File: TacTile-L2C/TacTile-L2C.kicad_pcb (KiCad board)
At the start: 2 copper layers, 25 x 25 mm, 2 parts, among them J1 Conn_01x05, J2 Conn_01x05

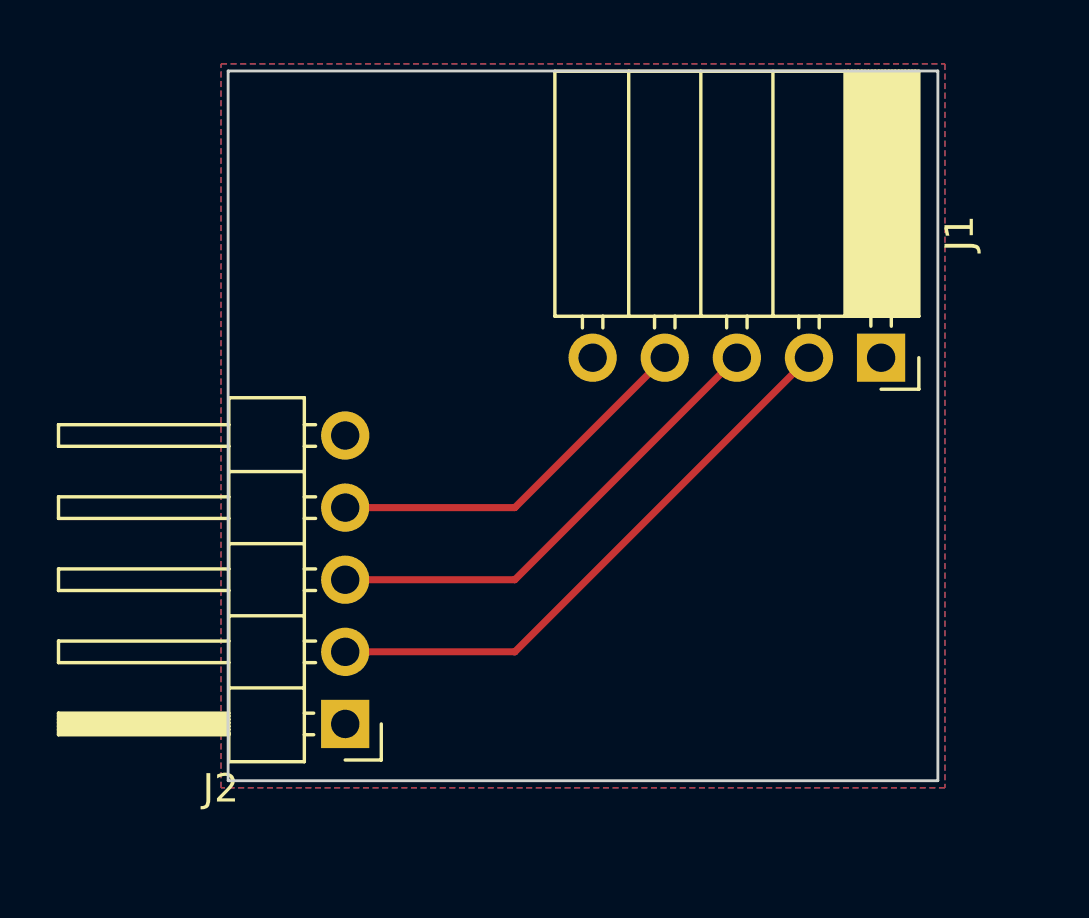
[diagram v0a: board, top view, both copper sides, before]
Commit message: Adjusted mounting for laser boards
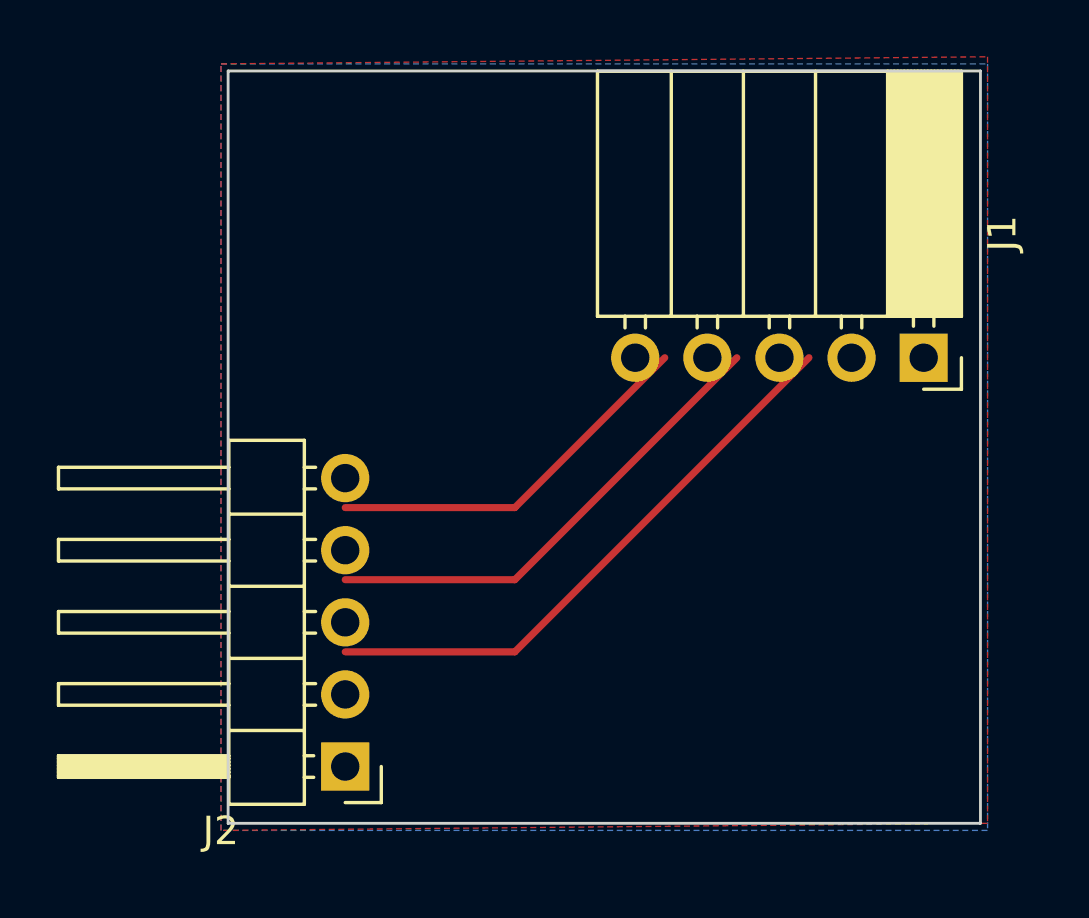
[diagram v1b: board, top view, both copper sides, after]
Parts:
- moved J1 1.50 mm to (49.5, 35.1)
- moved J2 1.50 mm to (29.1, 49.5)
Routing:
- net /SER: track 20.6 -> 0.00 mm
- net /VCC: track 0.00 -> 13.4 mm
- net /GND: track 13.4 -> 17.0 mm
- net /CLK: track 17.0 -> 20.6 mm
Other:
- board size 25 x 25 mm -> 26.5 x 26.5 mm
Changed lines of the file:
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@@
   (net 5 "/OUT")
   (footprint "Connector_PinSocket_2.54mm:PinSocket_1x05_P2.54mm_Horizontal" (layer "F.Cu")
-    (at 48 35.1 -90)
+    (at 49.5 35.1 -90)
     (descr "Through hole angled socket strip, 1x05, 2.54mm pitch, 8.51mm socket length, single row (from Kicad 4.0.7), script generated")
     (tags "Through hole angled socket strip THT 1x05 2.54mm single row")
@@
   )
   (footprint "Connector_PinHeader_2.54mm:PinHeader_1x05_P2.54mm_Horizontal" (layer "F.Cu")
-    (at 29.125 48 180)
+    (at 29.125 49.5 180)
     (descr "Through hole angled pin header, 1x05, 2.54mm pitch, 6mm pin length, single row")
     (tags "Through hole angled pin header THT 1x05 2.54mm single row")
@@
     )
   )
-  (gr_rect (start 25 25) (end 50 50)
+  (gr_rect (start 25 25) (end 51.5 51.5)
     (stroke (width 0.1) (type default)) (fill none) (layer "Edge.Cuts"))
-  (segment (start 40.38 35.1) (end 35.1 40.38) (width 0.25) (layer "F.Cu") (net 2))
-  (segment (start 35.1 40.38) (end 29.125 40.38) (width 0.25) (layer "F.Cu") (net 2))
-  (segment (start 42.92 35.1) (end 35.1 42.92) (width 0.25) (layer "F.Cu") (net 3))
-  (segment (start 35.1 42.92) (end 29.125 42.92) (width 0.25) (layer "F.Cu") (net 3))
-  (segment (start 45.46 35.1) (end 35.1 45.46) (width 0.25) (layer "F.Cu") (net 4))
-  (segment (start 35.1 45.46) (end 29.125 45.46) (width 0.25) (layer "F.Cu") (net 4))
+  (segment (start 40.38 35.1) (end 35.1 40.38) (width 0.25) (layer "F.Cu") (net 1))
+  (segment (start 35.1 40.38) (end 29.125 40.38) (width 0.25) (layer "F.Cu") (net 1))
+  (segment (start 42.92 35.1) (end 35.1 42.92) (width 0.25) (layer "F.Cu") (net 2))
+  (segment (start 35.1 42.92) (end 29.125 42.92) (width 0.25) (layer "F.Cu") (net 2))
+  (segment (start 45.46 35.1) (end 35.1 45.46) (width 0.25) (layer "F.Cu") (net 3))
+  (segment (start 35.1 45.46) (end 29.125 45.46) (width 0.25) (layer "F.Cu") (net 3))
   (zone (net 5) (net_name "/OUT") (layer "F.Cu") (hatch edge 0.5)
     (connect_pads (clearance 0.5))
@@
       (pts
         (xy 24.75 24.75)
-        (xy 50.25 24.75)
-        (xy 50.25 50.25)
-        (xy 24.75 50.25)
+        (xy 51.75 24.5)
+        (xy 51.75 51.5)
+        (xy 24.75 51.75)
       )
     )
@@
       (pts
         (xy 24.75 24.75)
-        (xy 50.25 24.75)
-        (xy 50.25 50.25)
-        (xy 24.75 50.25)
+        (xy 51.75 24.75)
+        (xy 51.75 51.75)
+        (xy 24.75 51.75)
       )
     )

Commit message: Updated more fabrication files and D board selecting wrong coil
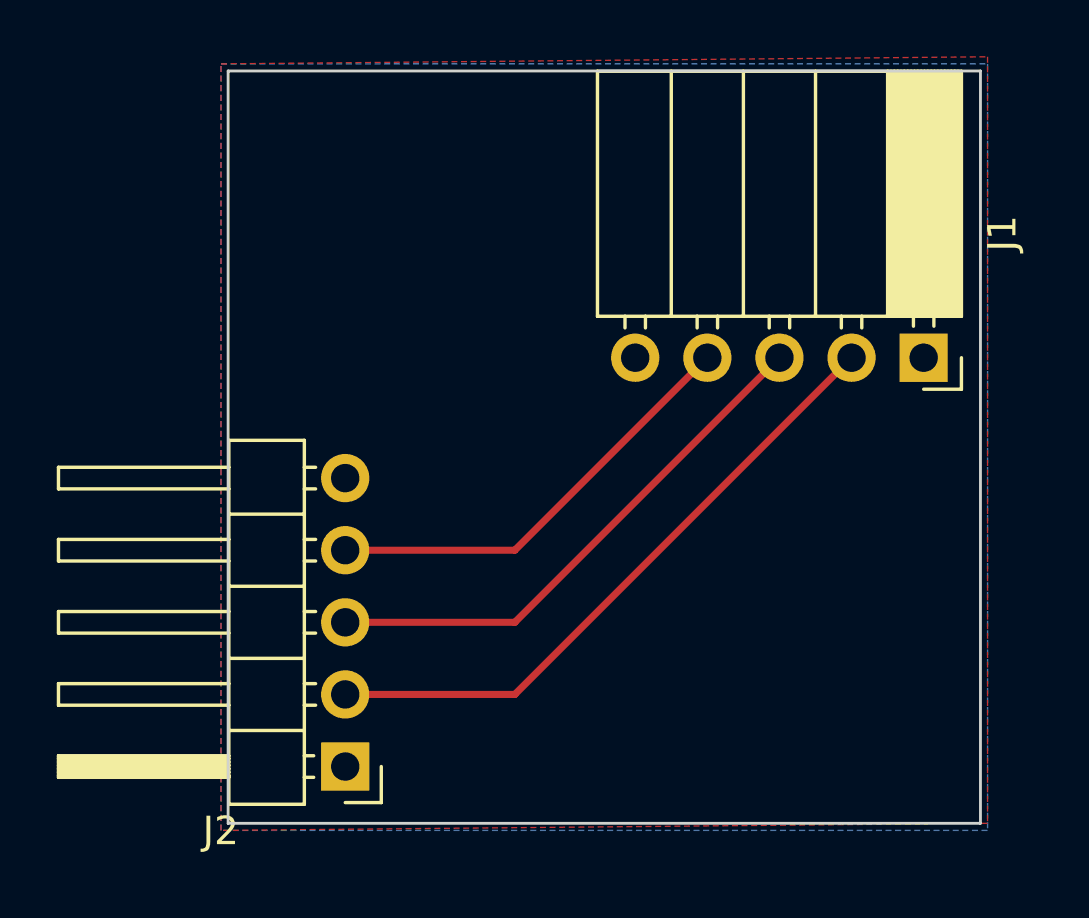
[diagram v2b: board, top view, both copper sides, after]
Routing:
- net /SER: track 0.00 -> 22.7 mm
- net /VCC: track 13.4 -> 0.00 mm
- net /GND: track 17.0 -> 15.6 mm
- net /CLK: track 20.6 -> 19.2 mm
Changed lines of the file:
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@@
       (drillshape 0)
       (scaleselection 1)
-      (outputdirectory "/fab")
+      (outputdirectory "./fab")
     )
   )
@@
   (gr_rect (start 25 25) (end 51.5 51.5)
     (stroke (width 0.1) (type default)) (fill none) (layer "Edge.Cuts"))
-  (segment (start 40.38 35.1) (end 35.1 40.38) (width 0.25) (layer "F.Cu") (net 1))
-  (segment (start 35.1 40.38) (end 29.125 40.38) (width 0.25) (layer "F.Cu") (net 1))
-  (segment (start 42.92 35.1) (end 35.1 42.92) (width 0.25) (layer "F.Cu") (net 2))
-  (segment (start 35.1 42.92) (end 29.125 42.92) (width 0.25) (layer "F.Cu") (net 2))
-  (segment (start 45.46 35.1) (end 35.1 45.46) (width 0.25) (layer "F.Cu") (net 3))
-  (segment (start 35.1 45.46) (end 29.125 45.46) (width 0.25) (layer "F.Cu") (net 3))
+  (segment (start 41.88 35.1) (end 35.1 41.88) (width 0.25) (layer "F.Cu") (net 2))
+  (segment (start 35.1 41.88) (end 29.125 41.88) (width 0.25) (layer "F.Cu") (net 2))
+  (segment (start 44.42 35.1) (end 35.1 44.42) (width 0.25) (layer "F.Cu") (net 3))
+  (segment (start 35.1 44.42) (end 29.125 44.42) (width 0.25) (layer "F.Cu") (net 3))
+  (segment (start 46.96 35.1) (end 35.1 46.96) (width 0.25) (layer "F.Cu") (net 4))
+  (segment (start 35.1 46.96) (end 29.125 46.96) (width 0.25) (layer "F.Cu") (net 4))
   (zone (net 5) (net_name "/OUT") (layer "F.Cu") (hatch edge 0.5)
     (connect_pads (clearance 0.5))
